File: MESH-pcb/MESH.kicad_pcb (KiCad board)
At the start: 2 copper layers, 61 parts, among them J1 Ant., J10 USB_C_Receptacle_USB2.0_16P, J2 Conn_01x08_Pin, J3 Conn_01x08_Pin, J4 Conn_01x08_Pin, J5 Conn_01x08_Pin, J6 Conn_01x05_Pin, J7 Conn_01x04_Pin, J8 Conn_01x02, J9 Conn_01x04_Pin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

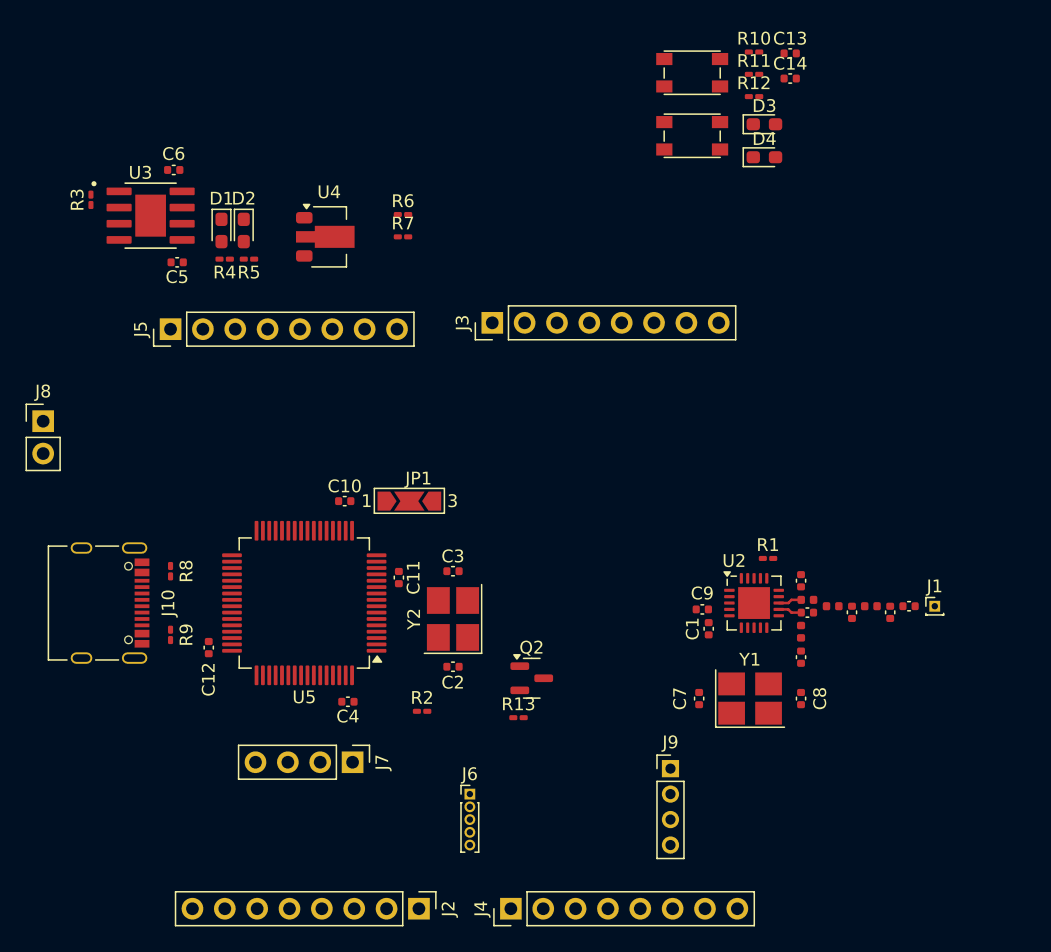
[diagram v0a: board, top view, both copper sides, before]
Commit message: Added custom component library, Almost final component placement
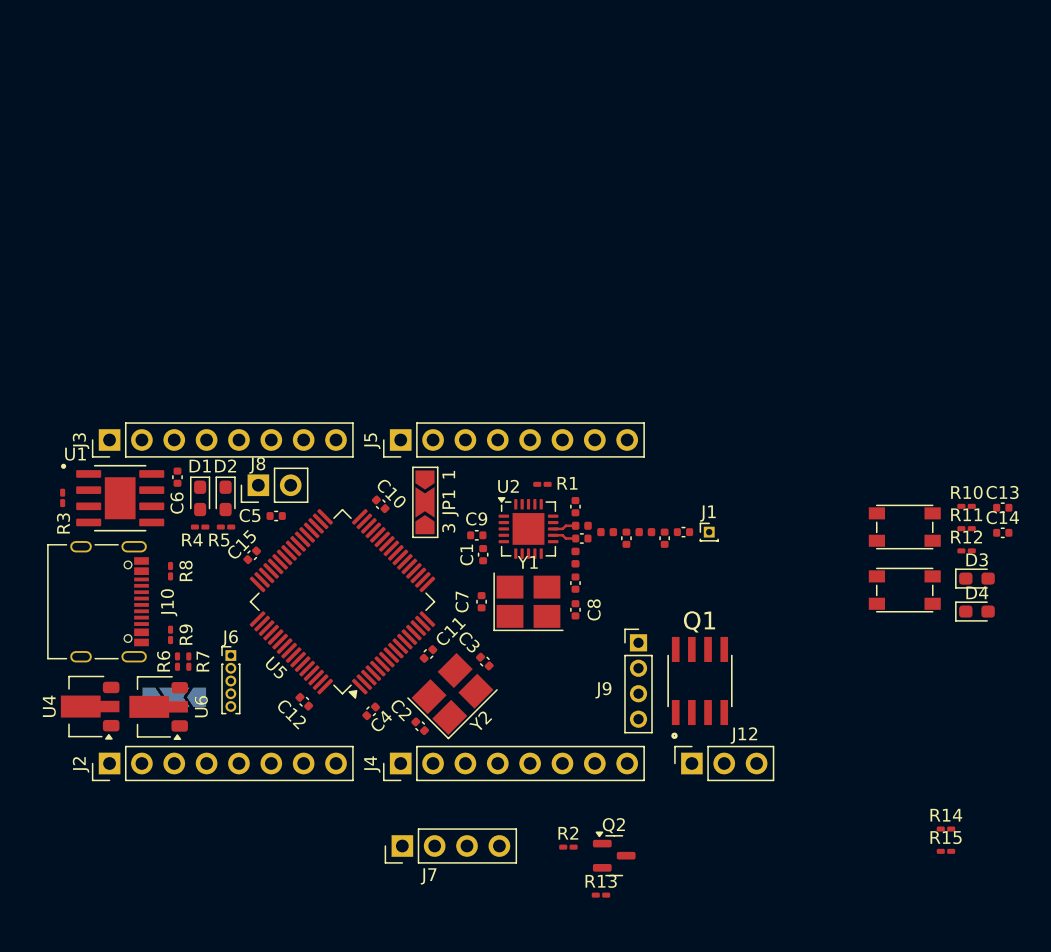
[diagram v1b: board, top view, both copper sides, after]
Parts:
- removed U3: TP4056, custom:SOP127P600X175-9N
- added C15: 10nF, Capacitor_SMD:C_0402_1005Metric, F.Cu at (111.9, 69.2)
- added J12: Conn_01x03_Pin, Connector_PinSocket_2.54mm:PinSocket_1x03_P2.54mm_Vertical, F.Cu at (146.4, 85.6)
- added JP2: A4/GND, Jumper:SolderJumper-3_P2.0mm_Open_TrianglePad1.0x1.5mm_NumberLabels, B.Cu at (105.8, 80.4)
- added Q1: NMOS, lib:SOIC127P600X175-8N, F.Cu at (147.1, 79.1)
- added R14: 220, Resistor_SMD:R_0201_0603Metric_Pad0.64x0.40mm_HandSolder, F.Cu at (166.4, 90.7)
- added R15: 1k, Resistor_SMD:R_0201_0603Metric_Pad0.64x0.40mm_HandSolder, F.Cu at (166.4, 92.5)
- added U1: TP4056, lib:SOP127P600X175-9N, F.Cu at (101.5, 64.8)
- added U6: AP2127R-3.3, Package_TO_SOT_SMD:SOT-89-3, F.Cu at (104.3, 81.2)
- moved U4 41.5 mm to (98.9, 81.1), turned to 180 degrees
- moved C13 39.4 mm to (170.8, 65.5)
- moved C14 39.4 mm to (170.8, 67.5)
- moved R10 39.4 mm to (168.0, 65.4)
- moved R11 39.4 mm to (168.0, 67.2)
- moved R12 39.4 mm to (168.0, 68.9)
- moved SW1 39.4 mm to (163.1, 67.1)
- moved SW2 39.4 mm to (163.1, 72.0)
- moved D3 39.4 mm to (168.8, 71.1)
- moved D4 39.4 mm to (168.8, 73.7)
- moved R6 39.3 mm to (106.0, 77.6), turned to 90 degrees
- moved R7 37.3 mm to (106.9, 77.6), turned to -90 degrees
- moved J3 31.4 mm to (100.7, 60.2)
- moved J2 26.8 mm to (100.7, 85.6), turned to 90 degrees
- moved C6 24.1 mm to (106.0, 63.1), turned to 90 degrees
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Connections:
- U5 pad 41: unconnected-(U5-PA8-Pad41) -> /CTRL
- U5 pad 48: VCC -> VDD_USB

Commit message: routing almost complete
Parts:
- removed J7: Conn_01x04_Pin, Connector_PinHeader_2.54mm:PinHeader_1x04_P2.54mm_Vertical
- added J11: Conn_01x02_Pin, Connector_PinHeader_2.54mm:PinHeader_1x02_P2.54mm_Vertical, F.Cu at (148.6, 73.5)
- C6, R3, U1, U4: moved to B.Cu
- moved SW1 64.8 mm to (99.8, 81.0)
- moved D4 64.5 mm to (105.0, 63.9)
- moved D3 64.0 mm to (105.0, 65.7)
- moved SW2 63.7 mm to (99.8, 64.8)
- moved C14 62.5 mm to (108.4, 69.3), turned to -90 degrees
- moved C13 60.6 mm to (112.5, 81.7)
- moved R10 58.5 mm to (109.6, 69.3), turned to 90 degrees
- moved R12 50.7 mm to (117.7, 62.8), turned to 180 degrees
- moved R11 50.4 mm to (117.7, 63.8), turned to 180 degrees
- moved R14 20.1 mm to (150.4, 78.6), turned to 90 degrees
- moved R15 19.7 mm to (150.4, 81.0), turned to 90 degrees
- moved R13 16.5 mm to (138.4, 79.5)
- moved Q2 15.9 mm to (138.4, 77.1), turned to 90 degrees
- moved R2 12.7 mm to (135.9, 79.5), turned to 180 degrees
- moved C6 8.48 mm to (97.6, 63.7), turned to -90 degrees
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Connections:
- J3 pad 7: VCC -> /SWCLK
- J3 pad 8: GND -> /SWDIO
- J4 pad 1: unconnected-(J4-Pin_1-Pad1) -> Net-(J4-Pin_1)
- J4 pad 2: unconnected-(J4-Pin_2-Pad2) -> Net-(J4-Pin_2)
- R2 pad 2: /RX2 -> Net-(U5-PA9)
- U1 pad 9: unconnected-(U1-EP-Pad9) -> GND
- U5 pad 42: unconnected-(U5-PA9-Pad42) -> Net-(U5-PA9)
- U5 pad 58: /I2C1_SCL -> Net-(J4-Pin_2)
- U5 pad 59: /I2C1_SDA -> Net-(J4-Pin_1)
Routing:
- net GND: track 0.00 -> 137.8 mm, vias 0 -> 17
- net VCC: track 0.00 -> 68.5 mm, vias 0 -> 10
- net /CTRL: track 0.00 -> 47.7 mm, vias 0 -> 2
- net /charger/Vcc: track 0.00 -> 47.3 mm, vias 0 -> 5
- net /charger/BAT: track 0.00 -> 44.9 mm, vias 0 -> 3
- net Net-(J5-Pin_8): track 0.00 -> 39.8 mm, vias 0 -> 2
- net Net-(J4-Pin_8): track 0.00 -> 37.9 mm, vias 0 -> 3
- net Net-(J5-Pin_7): track 0.00 -> 37.5 mm, vias 0 -> 2
- net Net-(J4-Pin_5): track 0.00 -> 29.2 mm, vias 0 -> 1
- net /SWDIO: track 0.00 -> 28.4 mm, vias 0 -> 2
- net Net-(J4-Pin_6): track 0.00 -> 27.8 mm, vias 0 -> 3
- net Net-(J2-Pin_1): track 0.00 -> 27.7 mm, vias 0 -> 4
- net Net-(J4-Pin_7): track 0.00 -> 27.1 mm, vias 0 -> 3
- net Net-(U5-PA9): track 0.00 -> 27.0 mm, vias 0 -> 2
- net Net-(J2-Pin_2): track 0.00 -> 27.0 mm, vias 0 -> 3
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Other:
- board outline added: 56.5 x 28.2 mm

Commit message: Ready to be exported
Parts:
- removed U6: AP2127R-3.3, Package_TO_SOT_SMD:SOT-89-3
- added Q3: NMOS, lib:SOIC127P600X175-8N, B.Cu at (147.1, 79.1)
- added R16: 220, Resistor_SMD:R_0201_0603Metric_Pad0.64x0.40mm_HandSolder, B.Cu at (150.4, 78.6)
- added R17: 1k, Resistor_SMD:R_0201_0603Metric_Pad0.64x0.40mm_HandSolder, B.Cu at (150.4, 81.0)
- added U3: AP2127K-3.3, Package_TO_SOT_SMD:SOT-23-5, F.Cu at (105.8, 80.5)
- R1, R10: footprint Capacitor_SMD:C_0201_0603Metric_Pad0.64x0.40mm_HandSolder -> Resistor_SMD:R_0201_0603Metric_Pad0.64x0.40mm_HandSolder
- U4: value AP2127R-3.3 -> AP2127K-3.3; footprint Package_TO_SOT_SMD:SOT-89-3 -> Package_TO_SOT_SMD:SOT-23-5
- moved U4 0.55 mm to (99.8, 80.8), turned to 180 degrees
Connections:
- net /CTRL renamed /CTRL1
- J12 pad 1: VCC -> GND
- J12 pad 2: GND -> Net-(J12-Pin_2)
- J4 pad 8: Net-(J4-Pin_8) -> unconnected-(J4-Pin_8-Pad8)
- U4 pad 1: GND -> /charger/BAT
- U4 pad 2: /charger/BAT -> GND
- U4 pad 3: VCC -> unconnected-(U4-EN-Pad3)
- U5 pad 26: Net-(J4-Pin_8) -> /CTRL2
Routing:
- net VCC: track 68.5 -> 171.0 mm, vias 10 -> 16
- net GND: track 137.8 -> 217.0 mm, vias 17 -> 73
- net /CTRL2: track 0.00 -> 50.5 mm, vias 0 -> 5
- net Net-(J4-Pin_8): track 37.9 -> 0.00 mm, vias 3 -> 0
- net Net-(Q3-G): track 0.00 -> 8.50 mm
- net /charger/Vcc: track 47.3 -> 43.9 mm
- net Net-(J2-Pin_3): track 25.2 -> 26.9 mm
- net Net-(U5-BOOT0): track 18.7 -> 20.3 mm
- net /CTRL1: track 47.7 -> 48.7 mm
- net /SWDIO: track 28.4 -> 27.6 mm
- net Net-(U5-PA9): track 27.0 -> 27.7 mm
- net Net-(J4-Pin_6): track 27.8 -> 28.4 mm
- net Net-(J4-Pin_7): track 27.1 -> 27.7 mm
- net Net-(J5-Pin_7): track 37.5 -> 38.1 mm
- net Net-(J10-CC2): track 1.83 -> 2.38 mm
- added copper zone on B.Cu, net GND
- added copper zone on F.Cu, net GND
- added copper zone on B.Cu, net Net-(J12-Pin_2)
- added copper zone on F.Cu, net Net-(J12-Pin_3)

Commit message: added pinheader footprint without outline, added pin names to silkscreen
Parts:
- J2, J3, J4, J5: footprint Connector_PinHeader_2.54mm:PinHeader_1x08_P2.54mm_Vertical -> lib:PinHeader_1x08_P2.54mm_Bare
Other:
- board text added: "PB0 PB1 PB2 PB3 PB4 PB5 PB6 PB7"
- board text added: "PB8 PB9 PB10 PB11 PB12 PB13 PB14 PB15"
- board text added: "PC7 PC6 PC5 PC4 PC3 PC2 PC1 PC0"
- board text added: "SWDIO SWCLK PC13 PC12 PC11 PC10 PC9 PC8"

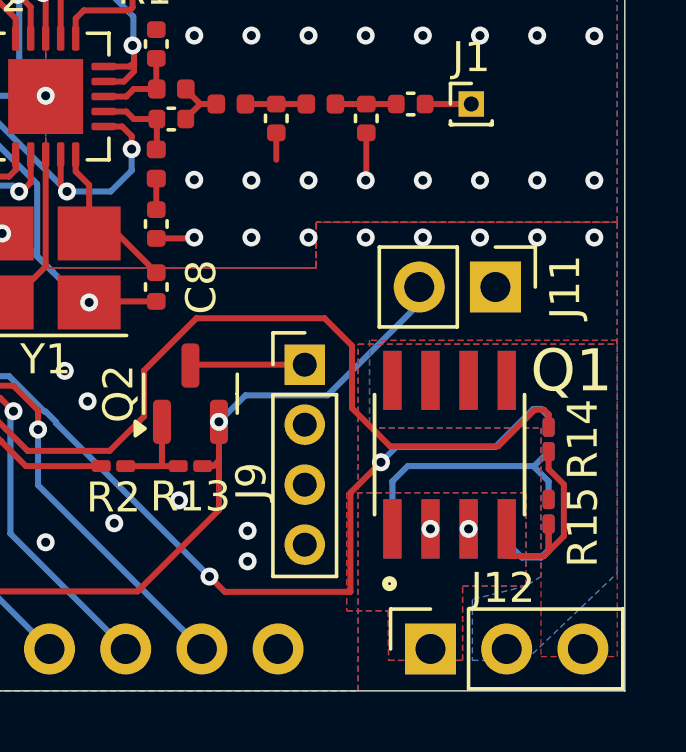
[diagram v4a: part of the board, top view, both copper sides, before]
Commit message: Added all pin names
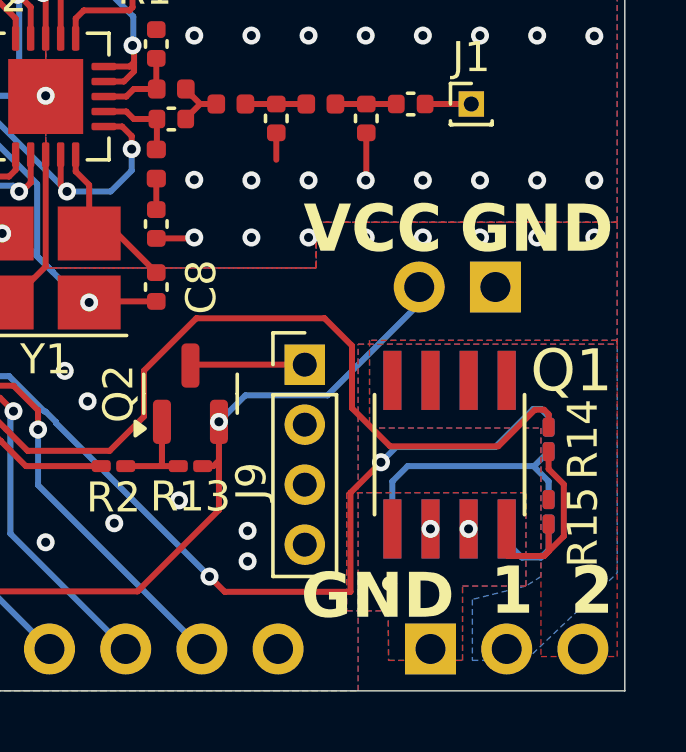
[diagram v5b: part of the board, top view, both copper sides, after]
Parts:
- J11: footprint Connector_PinHeader_2.54mm:PinHeader_1x02_P2.54mm_Vertical -> lib:PinHeader_1x02_P2.54mm_Bare
- J12: footprint Connector_PinSocket_2.54mm:PinSocket_1x03_P2.54mm_Vertical -> lib:PinHeader_1x03_P2.54mm_Bare
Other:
- board text added: "1"
- board text added: "2"
- board text added: "8"
- board text added: "9"
- board text added: "C0"
- board text added: "C1"
- board text added: "C2"
- board text added: "C3"
- board text added: "C4"
- board text added: "GND"
- board text added: "PB0"
- board text added: "PB1 PB2 PB3 PB4 PB5 PB6 PB7"
- board text added: "PC10"
- board text added: "PC11"
- board text added: "PC12"
- board text added: "PC13"
- board text added: "PC5"
- board text added: "PC7 PC6"
- board text added: "SWCLK"
- board text added: "SWDIO"
- board text added: "VCC"
- board text removed: "PB0 PB1 PB2 PB3 PB4 PB5 PB6 PB7"
- board text removed: "PC7 PC6 PC5 PC4 PC3 PC2 PC1 PC0"
- board text removed: "SWDIO SWCLK PC13 PC12 PC11 PC10 PC9 PC8"

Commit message: pcb ordered
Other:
- board text added: "+"
- board text added: "-"
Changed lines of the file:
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@@
 		(tags "resistor handsolder")
 		(property "Reference" "R10"
-			(at -2.286 -0.0254 90)
+			(at -2.3876 -0.0254 90)
 			(layer "F.SilkS")
 			(effects
@@
 		(tags "resistor handsolder")
 		(property "Reference" "R5"
-			(at 0 -0.911 0)
+			(at 0 -1.0888 0)
 			(layer "F.SilkS")
 			(effects
@@
 		(tags "resistor handsolder")
 		(property "Reference" "R4"
-			(at 0.635 -1.038 0)
+			(at 0.0254 -1.0888 0)
 			(layer "F.SilkS")
 			(effects
@@
 		(tags "capacitor")
 		(property "Reference" "C14"
-			(at 2.286 0.0254 270)
+			(at 2.3876 0.0254 270)
 			(layer "F.SilkS")
 			(effects
@@
 	)
 	(gr_text "PC5\n"
-		(at 112.395 80.264 270)
+		(at 112.395 80.1624 270)
 		(layer "B.SilkS")
 		(effects
@@
 	)
 	(gr_text "PB0"
-		(at 139.7 80.264 270)
+		(at 139.7 80.1624 270)
 		(layer "B.SilkS")
 		(effects
@@
 	)
 	(gr_text "PC7\nPC6\n"
-		(at 114.808 80.264 270)
+		(at 114.808 80.1624 270)
 		(layer "B.SilkS")
 		(effects
@@
 	)
 	(gr_text "C4"
-		(at 109.855 81.661 270)
+		(at 109.855 81.534 270)
 		(layer "B.SilkS")
 		(effects
@@
 	)
 	(gr_text "C2\n"
-		(at 104.775 81.661 270)
+		(at 104.775 81.534 270)
 		(layer "B.SilkS")
 		(effects
@@
 	)
 	(gr_text "C1\n"
-		(at 102.235 81.661 270)
+		(at 102.235 81.534 270)
 		(layer "B.SilkS")
 		(effects
@@
 	)
 	(gr_text "PB1\nPB2\nPB3\nPB4\nPB5\nPB6\nPB7"
-		(at 122.555 80.264 270)
+		(at 122.555 80.1624 270)
 		(layer "B.SilkS")
 		(effects
@@
 		)
 	)
+	(gr_text "+\n"
+		(at 113.03 63.246 0)
+		(layer "B.SilkS")
+		(effects
+			(font
+				(size 1.5 1.5)
+				(thickness 0.3)
+				(bold yes)
+			)
+			(justify left bottom mirror)
+		)
+	)
 	(gr_text "SWDIO\n"
 		(at 117.475 60.96 270)
@@
 		)
 	)
+	(gr_text "-"
+		(at 115.6208 63.246 0)
+		(layer "B.SilkS")
+		(effects
+			(font
+				(size 1.5 1.5)
+				(thickness 0.3)
+				(bold yes)
+			)
+			(justify left bottom mirror)
+		)
+	)
 	(gr_text "C3\n"
-		(at 107.442 81.661 270)
+		(at 107.442 81.534 270)
 		(layer "B.SilkS")
 		(effects
